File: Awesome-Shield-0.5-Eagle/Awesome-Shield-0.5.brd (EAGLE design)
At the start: 100 x 80 mm, 24 parts, among them J1 ARDUINO_R3_SHIELDUNO_R3_SHIEL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, SW1 SPST_TACT-EVQQ2

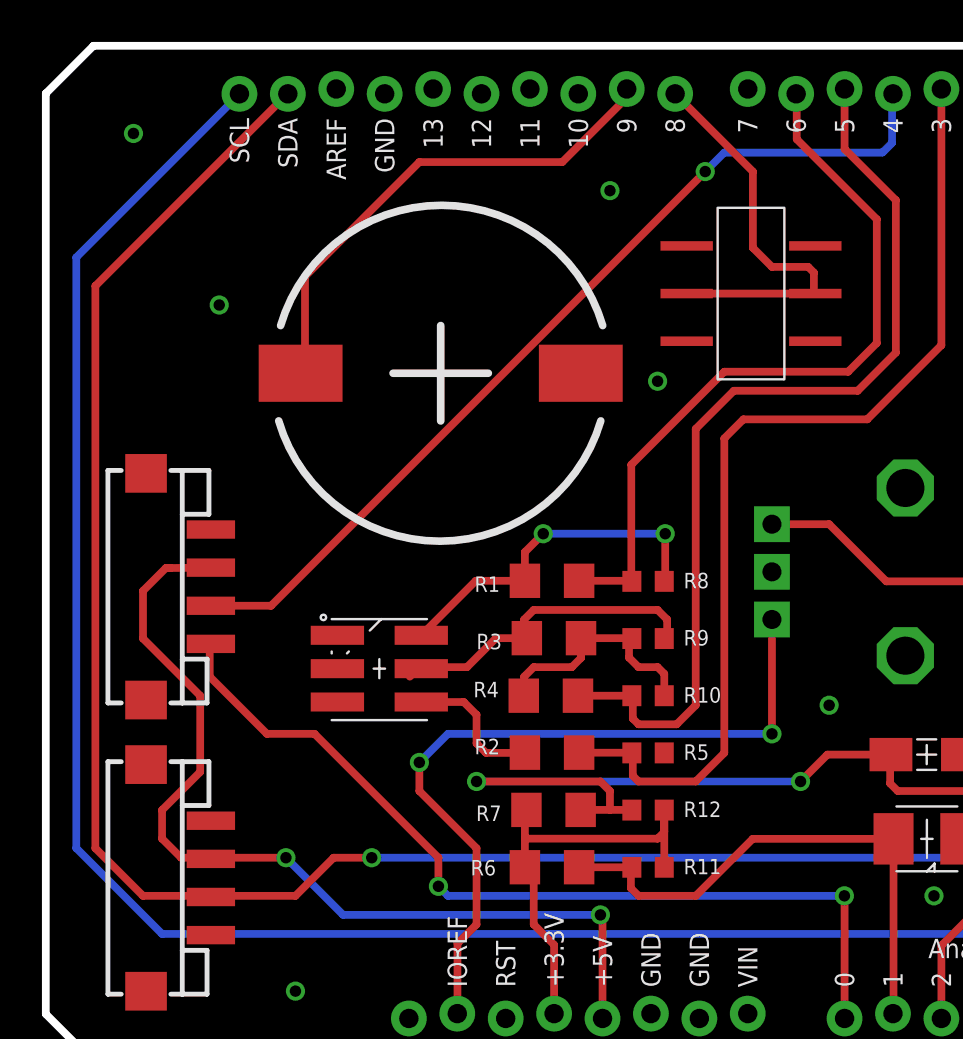
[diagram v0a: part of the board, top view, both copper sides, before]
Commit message: nudged resitor to remove unneeded vias, other tweaks
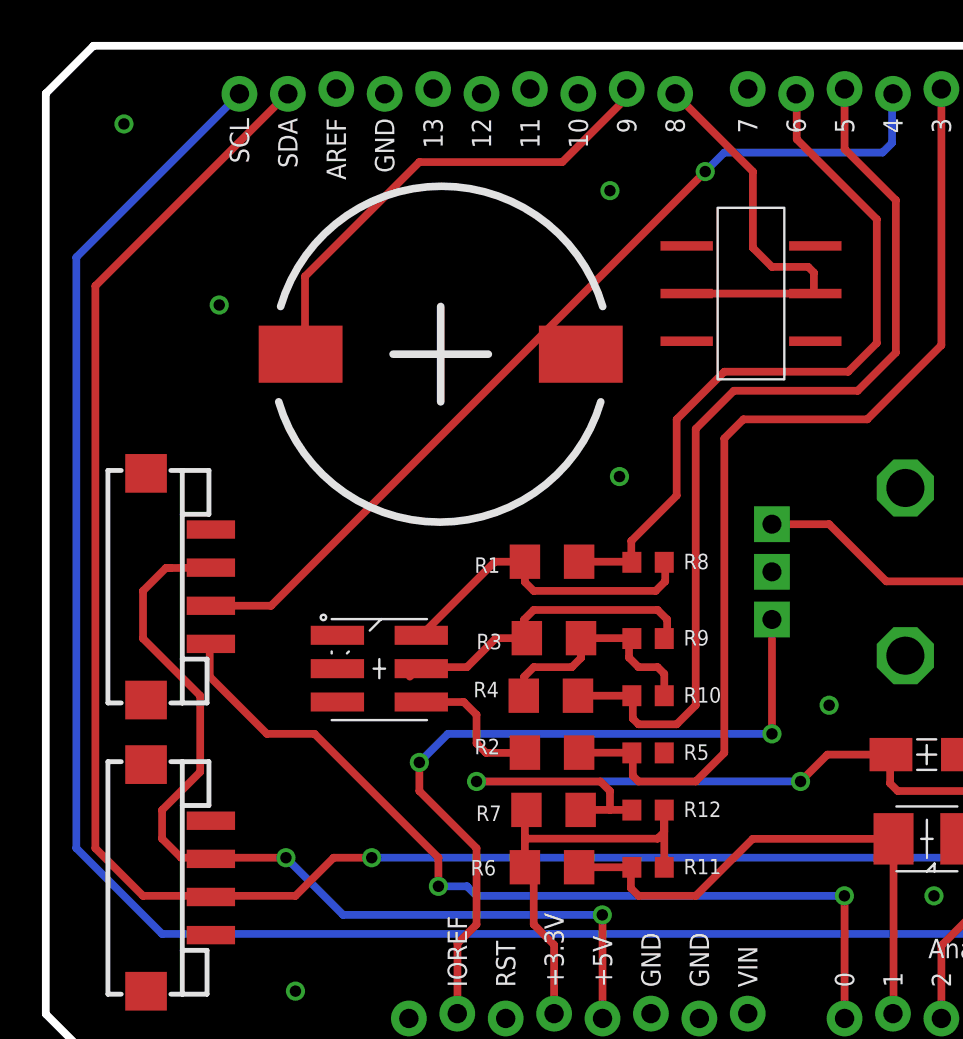
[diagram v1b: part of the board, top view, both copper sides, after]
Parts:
- moved R1 1.00 mm to (52.0, 44.0)
- moved R8 1.00 mm to (57.0, 44.0)
- moved SG1 1.00 mm to (46.1, 54.9)
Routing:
- net N$8: track 18.4 -> 16.9 mm, vias 2 -> 0
- net D6: track 39.2 -> 38.2 mm
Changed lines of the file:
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@@
 <attribute name="VALUE" x="72.63" y="30.69" size="0.4064" layer="27" rot="R180"/>
 </element>
-<element name="R1" library="rcl" package="R1206" value="" x="51.96" y="43.03" smashed="yes" rot="R180">
-<attribute name="NAME" x="49.23" y="43.26" size="0.8128" layer="25" rot="R180"/>
-<attribute name="VALUE" x="53.23" y="45.57" size="1.27" layer="27" rot="R180"/>
+<element name="R1" library="rcl" package="R1206" value="" x="51.96" y="44.03" smashed="yes" rot="R180">
+<attribute name="NAME" x="49.23" y="44.26" size="0.8128" layer="25" rot="R180"/>
+<attribute name="VALUE" x="53.23" y="46.57" size="1.27" layer="27" rot="R180"/>
 </element>
 <element name="R2" library="rcl" package="R1206" value="" x="51.96" y="34.01" smashed="yes" rot="R180">
@@
 <attribute name="VALUE" x="30.885" y="40.815" size="0.8128" layer="27" font="vector" ratio="10" rot="R90"/>
 </element>
-<element name="SG1" library="SparkFun-Electromechanical" package="BUZZER-CCV" value="BUZZERSMD2" x="46.12" y="53.92"/>
+<element name="SG1" library="SparkFun-Electromechanical" package="BUZZER-CCV" value="BUZZERSMD2" x="46.12" y="54.92"/>
 <element name="SJ1" library="SparkFun-Passives" package="PAD-JUMPER-2-NC_BY_TRACE_YES_SILK" value="JUMPER-PAD-2-NC_BY_TRACE" x="79" y="25.5" smashed="yes" rot="R270">
 <attribute name="NAME" x="77.27" y="25.9525" size="0.4064" layer="25" rot="R270"/>
@@
 <attribute name="VALUE" x="53.17" y="39.54" size="1.27" layer="27" rot="R180"/>
 </element>
-<element name="R8" library="rcl" package="R0603" value="" x="57" y="43" smashed="yes">
-<attribute name="NAME" x="58.865" y="42.635" size="0.8128" layer="25"/>
-<attribute name="VALUE" x="56.365" y="41.095" size="1.27" layer="27"/>
+<element name="R8" library="rcl" package="R0603" value="" x="57" y="44" smashed="yes">
+<attribute name="NAME" x="58.865" y="43.635" size="0.8128" layer="25"/>
+<attribute name="VALUE" x="56.365" y="42.095" size="1.27" layer="27"/>
 </element>
 <element name="R5" library="rcl" package="R0603" value="" x="57" y="34" smashed="yes">
@@
 <via x="81" y="42" extent="1-16" drill="0.6"/>
 <via x="38.5" y="21.5" extent="1-16" drill="0.6"/>
-<via x="57.5" y="53.5" extent="1-16" drill="0.6"/>
+<via x="55.5" y="48.5" extent="1-16" drill="0.6"/>
 <via x="55" y="63.5" extent="1-16" drill="0.6"/>
 <via x="72" y="26.5" extent="1-16" drill="0.6"/>
 <via x="66.5" y="36.5" extent="1-16" drill="0.6"/>
-<via x="30" y="66.5" extent="1-16" drill="0.6"/>
+<via x="29.5" y="67" extent="1-16" drill="0.6"/>
 </signal>
 <signal name="A2">
@@
 <wire x1="58" y1="40" x2="58" y2="41" width="0.4064" layer="1"/>
 <wire x1="58" y1="41" x2="57.5" y2="41.5" width="0.4064" layer="1"/>
-<wire x1="57.5" y1="41.5" x2="51" y2="41.5" width="0.4064" layer="1"/>
 <wire x1="51" y1="41.5" x2="50.5" y2="41" width="0.4064" layer="1"/>
 <wire x1="50.5" y1="41" x2="50.5" y2="40.158" width="0.4064" layer="1"/>
 <wire x1="50.5" y1="40.158" x2="50.638" y2="40.02" width="0.4064" layer="1"/>
+<wire x1="51" y1="41.5" x2="57.5" y2="41.5" width="0.4064" layer="1"/>
 <wire x1="45" y1="38.5" x2="45.1" y2="38.42" width="0" layer="19" extent="1-1"/>
 </signal>
@@
 <contactref element="J1" pad="D6"/>
 <contactref element="R8" pad="1"/>
-<wire x1="53.382" y1="43.03" x2="56.12" y2="43.03" width="0.4064" layer="1"/>
-<wire x1="56.12" y1="43.03" x2="56.15" y2="43" width="0.4064" layer="1"/>
-<wire x1="56.12" y1="43.03" x2="56.12" y2="49.12" width="0.4064" layer="1"/>
-<wire x1="56.12" y1="49.12" x2="61" y2="54" width="0.4064" layer="1"/>
+<wire x1="53.382" y1="44.03" x2="56.12" y2="44.03" width="0.4064" layer="1"/>
 <wire x1="61" y1="54" x2="67.5" y2="54" width="0.4064" layer="1"/>
 <wire x1="67.5" y1="54" x2="69" y2="55.5" width="0.4064" layer="1"/>
@@
 <wire x1="64.8" y1="66.2" x2="64.8" y2="68.55" width="0.4064" layer="1"/>
 <wire x1="64.8" y1="68.55" x2="64.77" y2="68.58" width="0.4064" layer="1"/>
+<wire x1="56.12" y1="44.03" x2="56.15" y2="44" width="0.4064" layer="1"/>
+<wire x1="56.12" y1="44.03" x2="56.12" y2="45.12" width="0.4064" layer="1"/>
+<wire x1="56.12" y1="45.12" x2="58.5" y2="47.5" width="0.4064" layer="1"/>
+<wire x1="58.5" y1="47.5" x2="58.5" y2="51.5" width="0.4064" layer="1"/>
+<wire x1="58.5" y1="51.5" x2="61" y2="54" width="0.4064" layer="1"/>
 </signal>
 <signal name="+5V">
@@
 <contactref element="J1" pad="5V"/>
 <wire x1="54.61" y1="20.066" x2="54.61" y2="25.39" width="0.4064" layer="1"/>
-<wire x1="54.61" y1="25.39" x2="54.5" y2="25.5" width="0.4064" layer="1"/>
-<via x="54.5" y="25.5" extent="1-16" drill="0.6"/>
-<wire x1="54.5" y1="25.5" x2="41" y2="25.5" width="0.4064" layer="16"/>
+<wire x1="54.61" y1="25.39" x2="54.6" y2="25.5" width="0.4064" layer="1"/>
+<via x="54.6" y="25.5" extent="1-16" drill="0.6"/>
+<wire x1="54.6" y1="25.5" x2="41" y2="25.5" width="0.4064" layer="16"/>
 <wire x1="41" y1="25.5" x2="38" y2="28.5" width="0.4064" layer="16"/>
 <via x="38" y="28.5" extent="1-16" drill="0.6"/>
@@
 <wire x1="67.31" y1="26.49" x2="67.3" y2="26.5" width="0.4064" layer="1"/>
 <via x="67.3" y="26.5" extent="1-16" drill="0.6"/>
-<wire x1="67.3" y1="26.5" x2="46.5" y2="26.5" width="0.4064" layer="16"/>
-<wire x1="46.5" y1="26.5" x2="46" y2="27" width="0.4064" layer="16"/>
+<wire x1="67.3" y1="26.5" x2="48" y2="26.5" width="0.4064" layer="16"/>
 <via x="46" y="27" extent="1-16" drill="0.6"/>
 <wire x1="46" y1="27" x2="46" y2="28.5" width="0.4064" layer="1"/>
@@
 <wire x1="34" y1="38" x2="34" y2="39.66" width="0.4064" layer="1"/>
 <wire x1="34" y1="39.66" x2="34.06" y2="39.72" width="0.4064" layer="1"/>
+<wire x1="46" y1="27" x2="47.5" y2="27" width="0.4064" layer="16"/>
+<wire x1="47.5" y1="27" x2="48" y2="26.5" width="0.4064" layer="16"/>
 </signal>
 <signal name="A5">
@@
 <wire x1="45" y1="65" x2="39" y2="59" width="0.4064" layer="1"/>
 <wire x1="39" y1="59" x2="39" y2="54.15" width="0.4064" layer="1"/>
-<wire x1="39" y1="54.15" x2="38.77" y2="53.92" width="0.4064" layer="1"/>
+<wire x1="39" y1="54.15" x2="38.77" y2="54.92" width="0.4064" layer="1"/>
 </signal>
 <signal name="D4">
@@
 <contactref element="R8" pad="2"/>
 <contactref element="R1" pad="2"/>
-<wire x1="50.538" y1="43.03" x2="47.96" y2="43.03" width="0.4064" layer="1"/>
-<wire x1="47.96" y1="43.03" x2="45.1" y2="40.17" width="0.4064" layer="1"/>
-<wire x1="50.538" y1="43.03" x2="50.538" y2="44.538" width="0.4064" layer="1"/>
-<wire x1="50.538" y1="44.538" x2="51.5" y2="45.5" width="0.4064" layer="1"/>
-<via x="51.5" y="45.5" extent="1-16" drill="0.6"/>
-<wire x1="51.5" y1="45.5" x2="57.9" y2="45.5" width="0.4064" layer="16"/>
-<via x="57.9" y="45.5" extent="1-16" drill="0.6"/>
-<wire x1="57.9" y1="45.5" x2="57.9" y2="43.05" width="0.4064" layer="1"/>
-<wire x1="57.9" y1="43.05" x2="57.85" y2="43" width="0.4064" layer="1"/>
+<wire x1="50.538" y1="44.03" x2="48.96" y2="44.03" width="0.4064" layer="1"/>
+<wire x1="48.96" y1="44.03" x2="45.1" y2="40.17" width="0.4064" layer="1"/>
+<wire x1="50.538" y1="44.03" x2="50.538" y2="42.962" width="0.4064" layer="1"/>
+<wire x1="50.538" y1="42.962" x2="51" y2="42.5" width="0.4064" layer="1"/>
+<wire x1="51" y1="42.5" x2="57.4" y2="42.5" width="0.4064" layer="1"/>
+<wire x1="57.4" y1="42.5" x2="57.9" y2="43" width="0.4064" layer="1"/>
+<wire x1="57.9" y1="43" x2="57.9" y2="43.95" width="0.4064" layer="1"/>
+<wire x1="57.9" y1="43.95" x2="57.85" y2="44" width="0.4064" layer="1"/>
 </signal>
 <signal name="D3">

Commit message: fixed overlap as per DRC
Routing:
- net D4: track 48.4 -> 50.7 mm
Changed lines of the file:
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@@
 <via x="38.5" y="21.5" extent="1-16" drill="0.6"/>
 <via x="55.5" y="48.5" extent="1-16" drill="0.6"/>
-<via x="55" y="63.5" extent="1-16" drill="0.6"/>
+<via x="87.5" y="73" extent="1-16" drill="0.6"/>
 <via x="72" y="26.5" extent="1-16" drill="0.6"/>
 <via x="66.5" y="36.5" extent="1-16" drill="0.6"/>
@@
 <contactref element="J2" pad="2"/>
 <wire x1="34.06" y1="41.72" x2="37.22" y2="41.72" width="0.4064" layer="1"/>
-<wire x1="37.22" y1="41.72" x2="60" y2="64.5" width="0.4064" layer="1"/>
 <via x="60" y="64.5" extent="1-16" drill="0.6"/>
 <wire x1="60" y1="64.5" x2="61" y2="65.5" width="0.4064" layer="16"/>
@@
 <wire x1="69.8" y1="66" x2="69.8" y2="68.53" width="0.4064" layer="16"/>
 <wire x1="69.8" y1="68.53" x2="69.85" y2="68.58" width="0.4064" layer="16"/>
+<wire x1="49.5" y1="58" x2="49" y2="57.5" width="0.4064" layer="1"/>
+<wire x1="49" y1="57.5" x2="41.5" y2="50" width="0.4064" layer="1"/>
+<wire x1="41.5" y1="50" x2="41.5" y2="46" width="0.4064" layer="1"/>
+<wire x1="41.5" y1="46" x2="37.22" y2="41.72" width="0.4064" layer="1"/>
+<wire x1="60" y1="64.5" x2="56" y2="64.5" width="0.4064" layer="1"/>
+<wire x1="56" y1="64.5" x2="49.5" y2="58" width="0.4064" layer="1"/>
 </signal>
 <signal name="N$2">

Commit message: nudged traces
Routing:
- net D9: track 26.9 -> 25.0 mm
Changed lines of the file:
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@@
 <via x="66.5" y="36.5" extent="1-16" drill="0.6"/>
 <via x="29.5" y="67" extent="1-16" drill="0.6"/>
+<wire x1="79.78" y1="62.58" x2="87.5" y2="73" width="0" layer="19" extent="1-1"/>
 </signal>
 <signal name="A2">
@@
 <contactref element="J1" pad="D9"/>
 <contactref element="SG1" pad="-"/>
-<wire x1="55.88" y1="68.834" x2="55.88" y2="68.38" width="0.4064" layer="1"/>
-<wire x1="55.88" y1="68.38" x2="52.5" y2="65" width="0.4064" layer="1"/>
-<wire x1="52.5" y1="65" x2="45" y2="65" width="0.4064" layer="1"/>
-<wire x1="45" y1="65" x2="39" y2="59" width="0.4064" layer="1"/>
-<wire x1="39" y1="59" x2="39" y2="54.15" width="0.4064" layer="1"/>
-<wire x1="39" y1="54.15" x2="38.77" y2="54.92" width="0.4064" layer="1"/>
+<wire x1="55.88" y1="68.834" x2="55.88" y2="65.28" width="0.4064" layer="1"/>
+<wire x1="45.5" y1="54.9" x2="38.79" y2="54.9" width="0.4064" layer="1"/>
+<wire x1="38.79" y1="54.9" x2="38.77" y2="54.92" width="0.4064" layer="1"/>
+<wire x1="55.88" y1="65.28" x2="45.5" y2="54.9" width="0.4064" layer="1"/>
 </signal>
 <signal name="D4">
@@
 <wire x1="69.8" y1="66" x2="69.8" y2="68.53" width="0.4064" layer="16"/>
 <wire x1="69.8" y1="68.53" x2="69.85" y2="68.58" width="0.4064" layer="16"/>
-<wire x1="49.5" y1="58" x2="49" y2="57.5" width="0.4064" layer="1"/>
-<wire x1="49" y1="57.5" x2="41.5" y2="50" width="0.4064" layer="1"/>
-<wire x1="41.5" y1="50" x2="41.5" y2="46" width="0.4064" layer="1"/>
+<wire x1="41.5" y1="49.5" x2="41.5" y2="46" width="0.4064" layer="1"/>
 <wire x1="41.5" y1="46" x2="37.22" y2="41.72" width="0.4064" layer="1"/>
-<wire x1="60" y1="64.5" x2="56" y2="64.5" width="0.4064" layer="1"/>
-<wire x1="56" y1="64.5" x2="49.5" y2="58" width="0.4064" layer="1"/>
+<wire x1="60" y1="64.5" x2="56.5" y2="64.5" width="0.4064" layer="1"/>
+<wire x1="56.5" y1="64.5" x2="41.5" y2="49.5" width="0.4064" layer="1"/>
 </signal>
 <signal name="N$2">

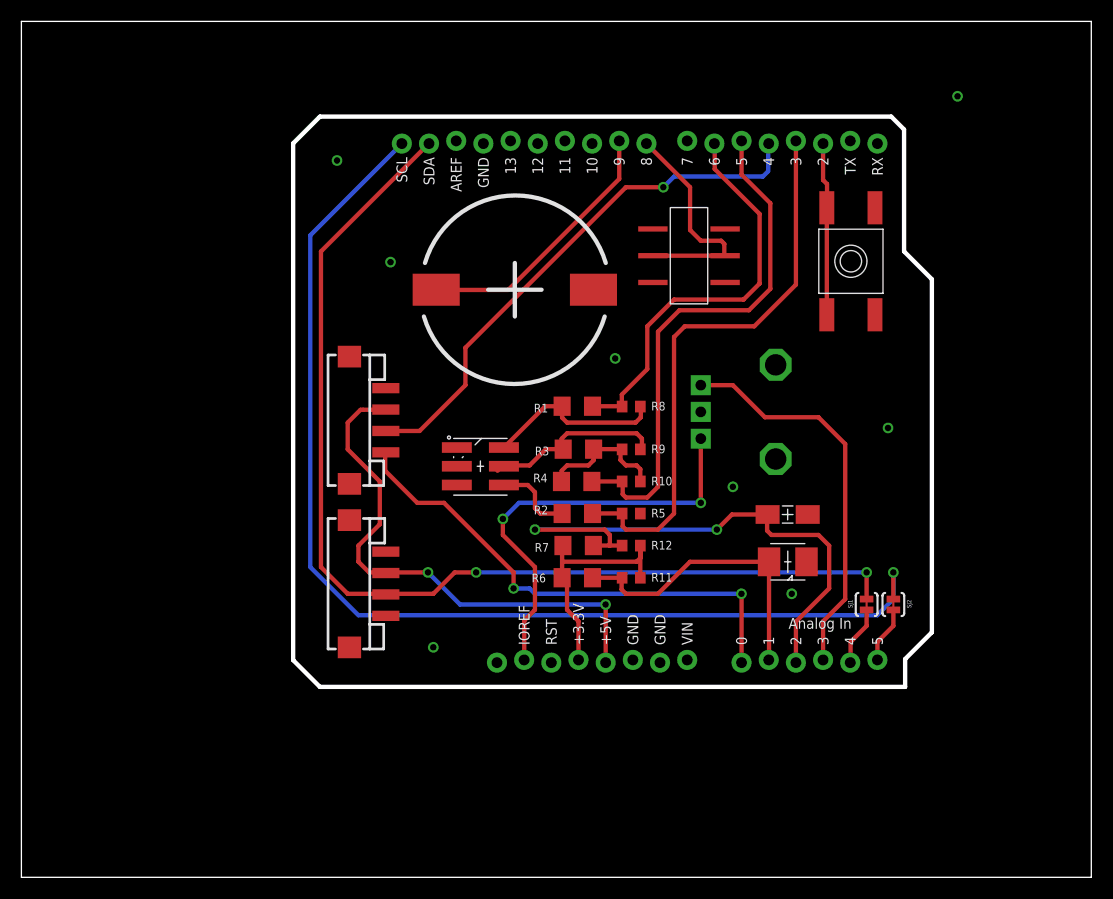
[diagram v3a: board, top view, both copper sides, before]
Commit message: redrew board outline to avoid USB and power connectors so that short male headers can be used, layout runs off not yet adjusted to fit new board shape and size
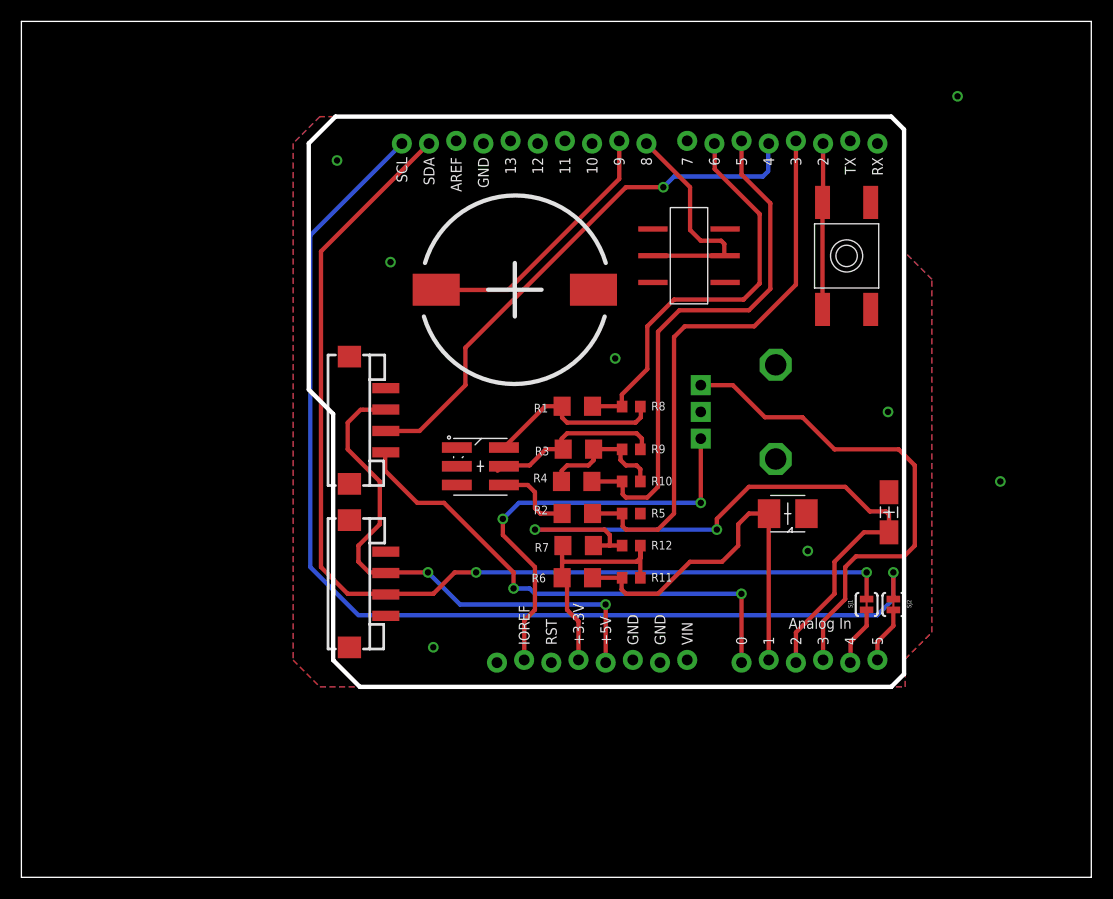
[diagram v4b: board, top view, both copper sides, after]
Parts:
- moved F1 9.47 mm to (81.1, 34.1), turned to 270 degrees
- moved Q1 4.50 mm to (71.6, 34.0)
- moved SW1 0.64 mm to (77.1, 58.1)
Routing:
- net A2: track 53.3 -> 66.1 mm
- net A3: track 36.8 -> 47.5 mm
- net A1: track 28.3 -> 35.8 mm
- net D2: track 16.5 -> 15.5 mm
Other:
- outline, holes or cut-outs redrawn

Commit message: adjusted layout to accomodate smaller board size
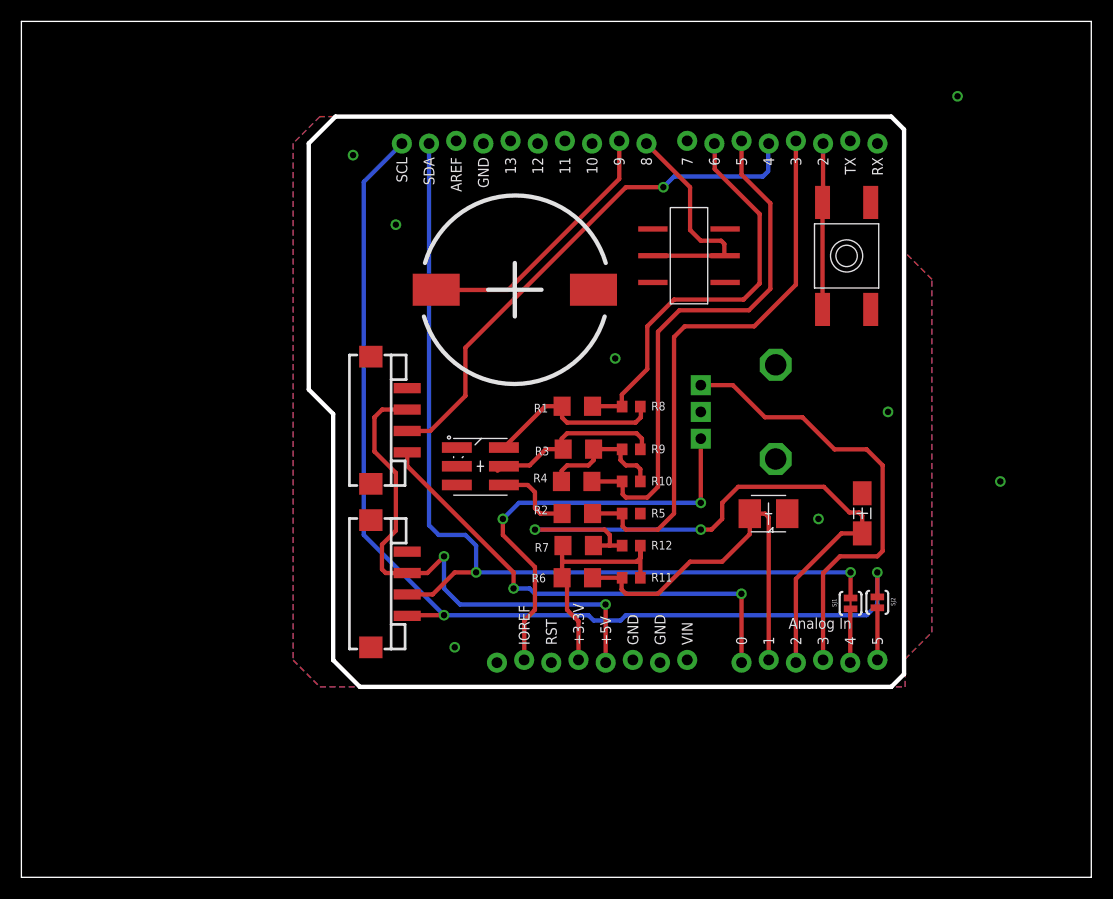
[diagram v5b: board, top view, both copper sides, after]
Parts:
- moved F1 2.50 mm to (78.6, 34.0)
- moved J2 2.00 mm to (36.1, 42.7)
- moved J5 2.00 mm to (36.1, 27.4)
- moved Q1 1.80 mm to (69.8, 34.0)
- moved SJ2 1.51 mm to (80.0, 25.7)
- moved SJ1 1.50 mm to (77.5, 25.6)
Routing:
- net SDA: track 99.2 -> 88.1 mm
- net SCL: track 105.3 -> 98.7 mm, vias 1 -> 2
- net A3: track 47.5 -> 42.6 mm
- net A2: track 66.1 -> 62.6 mm
- net A0: track 47.1 -> 44.8 mm
- net D4: track 50.4 -> 49.0 mm
- net A4: track 5.60 -> 5.04 mm
